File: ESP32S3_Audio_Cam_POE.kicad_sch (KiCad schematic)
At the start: 499 parts, among them CN1 PJ-316C-6A, J1 Connector, USB-TYPE-C-16P, J10 Conn_01x02, J11 Conn_01x02, J12 Conn_01x02, J13 Conn_01x02, J14 Conn_01x02, J15 Conn_01x02, J16 Conn_01x02, J17 Conn_01x02, J18 Conn_01x02, J19 Conn_01x02, J2 Connector, USB-TYPE-C-16P, J3 Conn_01x02, J4 Conn_01x02, J5 Conn_01x03, J6 Conn_01x03, J7 Conn_01x03, J8 Conn_01x03, J9 HC-RJ45-055-4_8P8C_Shielded, Q1 AO3401A, Q2 AO3401A, Q3 AO3401A, Q4 AO3401A, Q5 AO3401A, Q6 AO3401A, Q7 AO3401A, Q8 AO3401A, T1 H1102NLT, U1 TLV62568DBVR, U10 W25Q128JVSIQ, U11 TM1637, U12 DS18B20U(UMW), U13 W25Q128JVSIQ, U14 DP9900M-5V, U15 MAX98357AETE+T, U16 MSM261S4030H0R, U17 MSM261S4030H0R, U18 AXP2101, U19 RFM69HCW, U2 MT9221CT-06BR5, U3 USBLC6-2SC6, U4 USBLC6-2SC6, U5 XC6206-1.5NR, U6 XC6206-2.8V, U7 ESP32-S3, U8 ESP32-S3, U9 W5500, X1 X322525MOB4SI, Y1 40MHz, 15pF, Y2 40MHz, 15pF, Y3 32.768KHz

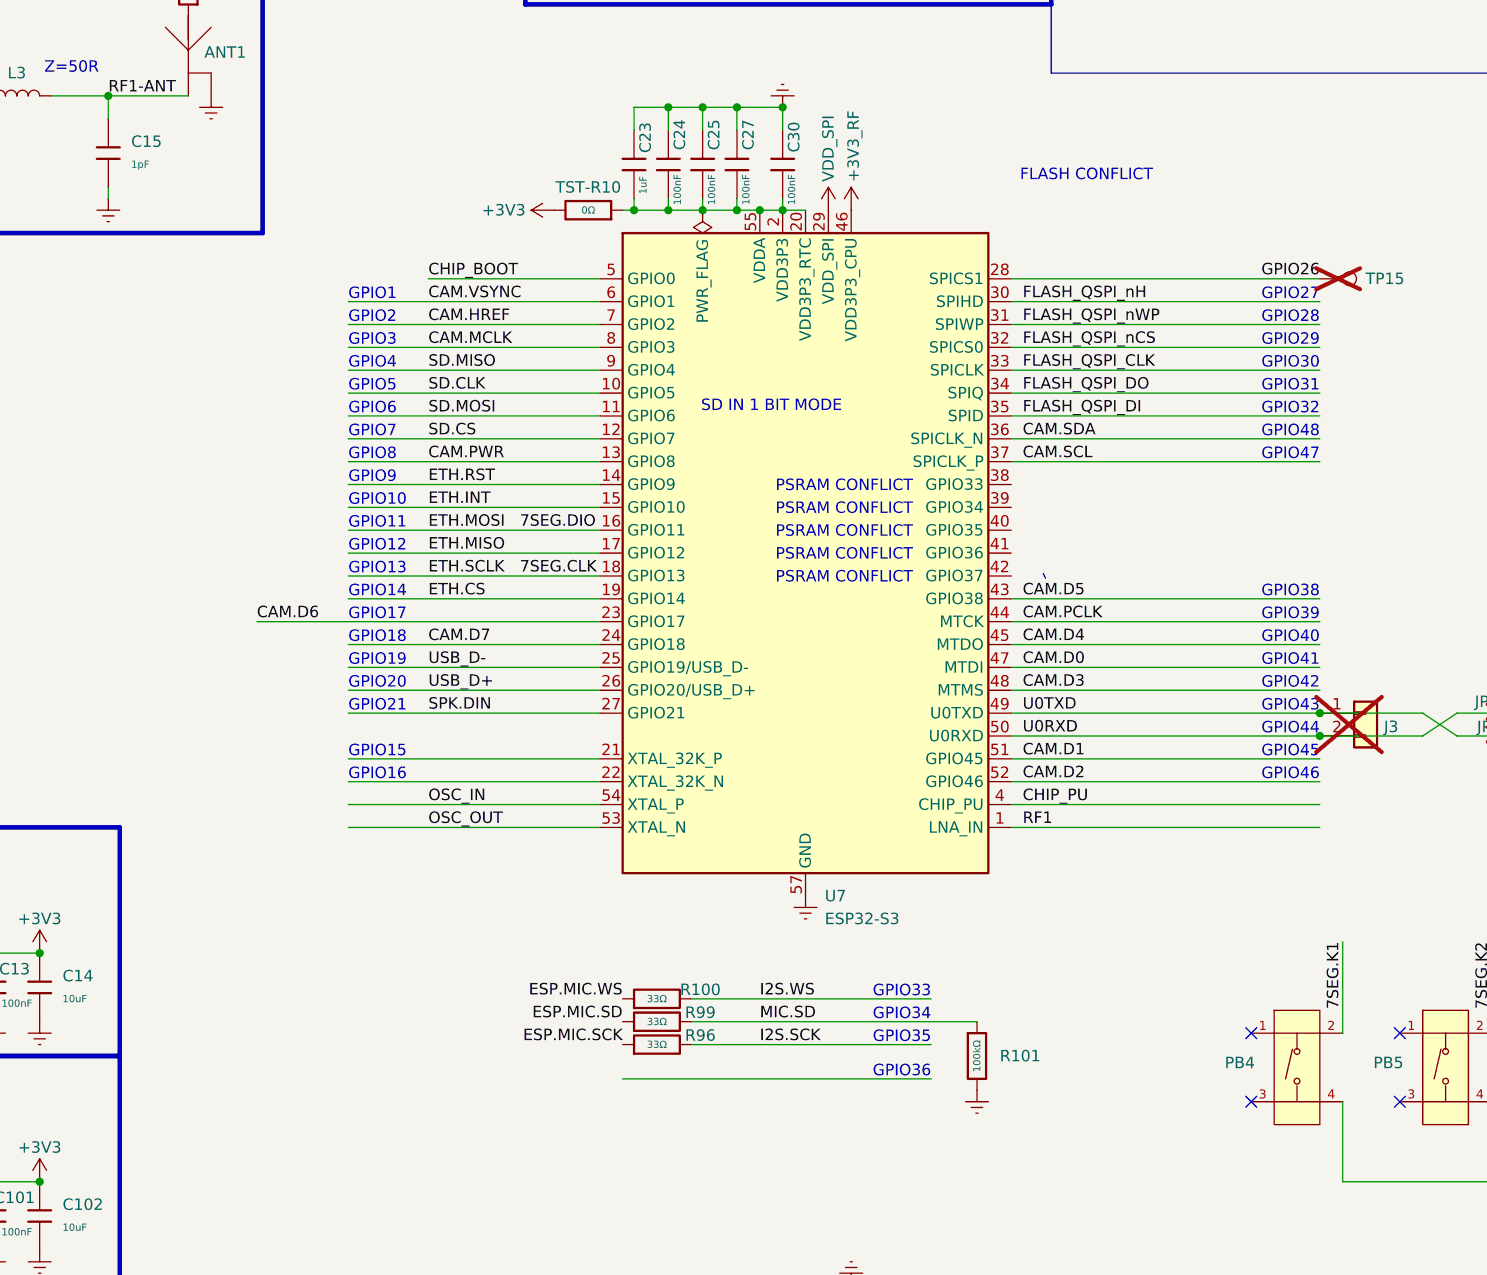
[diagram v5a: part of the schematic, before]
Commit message: re-connected digital signals now without conflict on PSRAM IO. Layout needs updating.
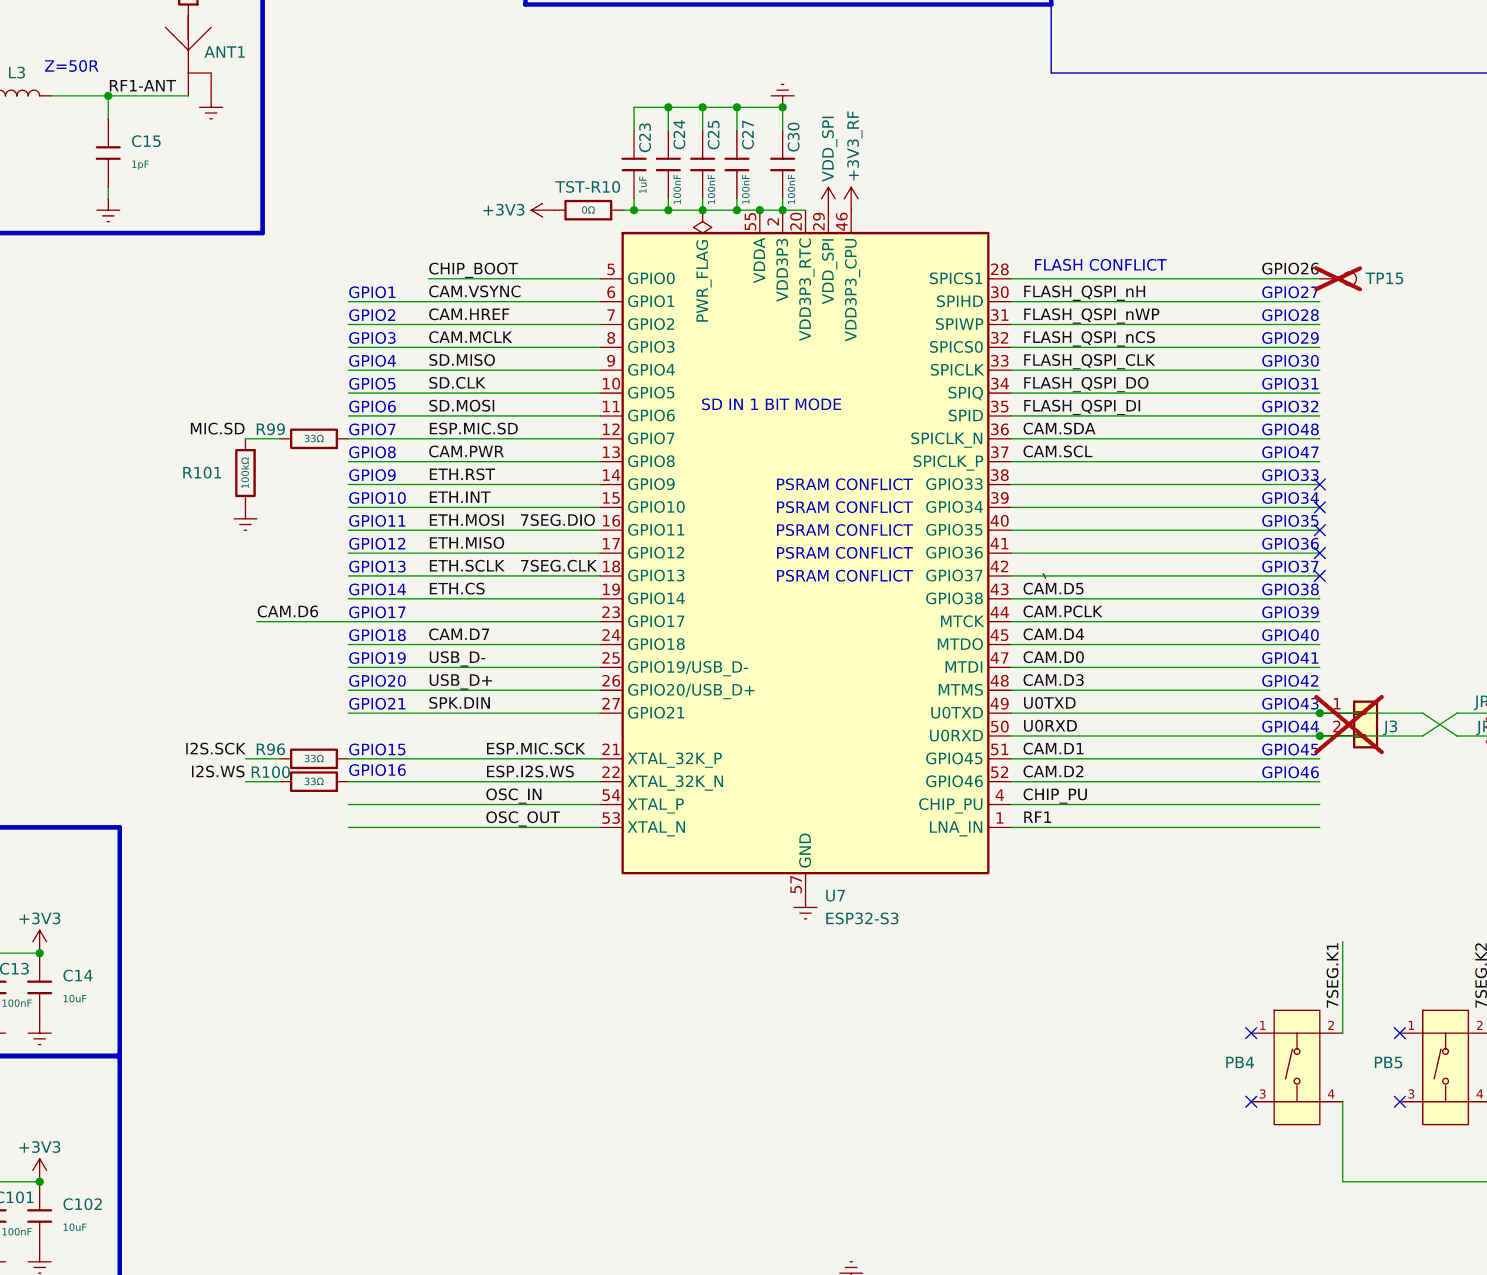
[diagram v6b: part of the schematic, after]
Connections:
- net ESP.MIC.WS is gone; now on net ESP.I2S.WS: R100.1
- net ESP.MIC.SCK: now also U7.21 (XTAL_32K_P)
- net ESP.MIC.SD: now also U7.12 (GPIO7)
- net SD.CS: no longer U7.12 (GPIO7)
- net ESP.I2S.WS: now reaches U7.22 (XTAL_32K_N)
- no-connect marks 36 -> 41
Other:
- note added: "GPIO37"
- moved on the sheet: R100, R101, R96, R99

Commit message: updated pin out layout is now off of PSRAM IO.
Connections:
- net CAM.D6: now also U7.12 (GPIO7); no longer U7.23 (GPIO17)
- net CAM.D7: now also U7.13 (GPIO8); no longer U7.24 (GPIO18)
- net CAM.PWR: now also U7.21 (XTAL_32K_P); no longer U7.13 (GPIO8)
- net ESP.I2S.WS: now also U7.24 (GPIO18); no longer U7.22 (XTAL_32K_N)
- net ESP.MIC.SCK: now also U7.22 (XTAL_32K_N); no longer U7.21 (XTAL_32K_P)
- net ESP.MIC.SD: now also U7.23 (GPIO17); no longer U7.12 (GPIO7)
- no-connect marks 41 -> 40
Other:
- moved on the sheet: R100, R101, R96, R99

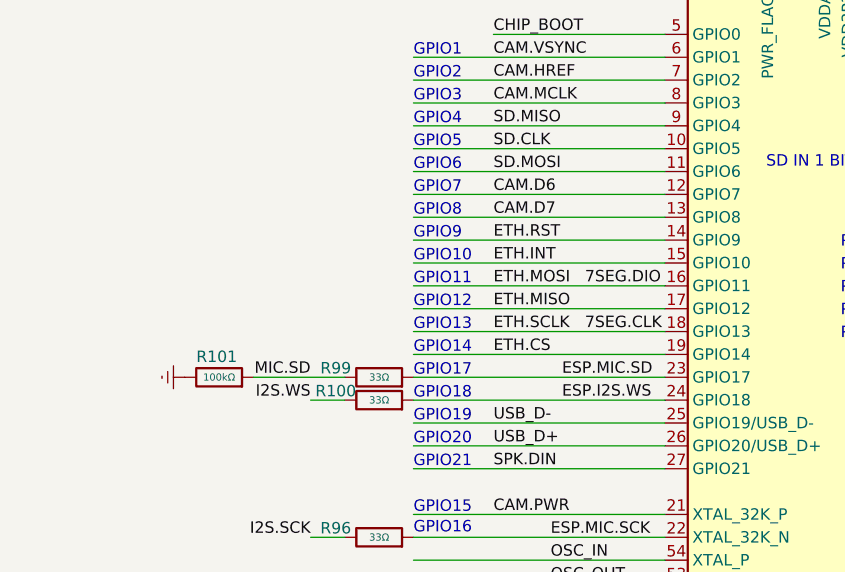
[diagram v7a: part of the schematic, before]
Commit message: flipped D6 and D7 back to original pins, needed for internal connects.
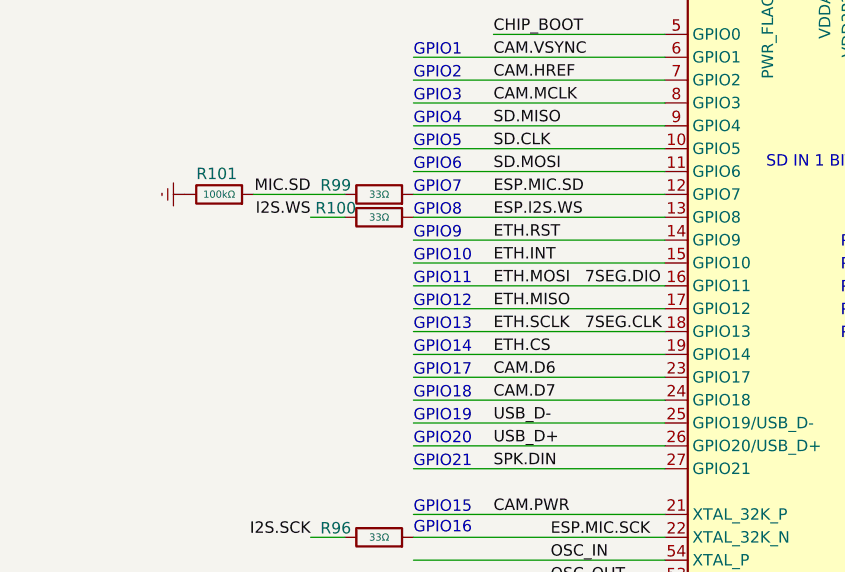
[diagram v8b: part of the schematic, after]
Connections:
- net CAM.D6: now also U7.23 (GPIO17); no longer U7.12 (GPIO7)
- net CAM.D7: now also U7.24 (GPIO18); no longer U7.13 (GPIO8)
- net ESP.I2S.WS: now also U7.13 (GPIO8); no longer U7.24 (GPIO18)
- net ESP.MIC.SD: now also U7.12 (GPIO7); no longer U7.23 (GPIO17)
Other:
- moved on the sheet: R100, R101, R99
